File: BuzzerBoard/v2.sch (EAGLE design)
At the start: 9 parts, among them J1 p0, U1 LM386MX-1/NOPB

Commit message: starting on v2
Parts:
- removed R1: 23BR100KLFTR, BuzzerLib:23BR100KLFTR
- removed U$1: SMS-1308MS-2-R, BuzzerLib:SMS-1308MS-2-R
- added C5: GRM188R60J106ME47D, BuzzerLib:GRM188R60J106ME47D
- added C6: C2012X5R1A336M125AC, BuzzerLib:C2012X5R1A336M125AC
- added J2: (no value), SparkFun-Connectors:CONN_02
- added U2: Value, BuzzerLib:TPS63001DRCR
- added U3: LQM2HPN1R5MG0L, BuzzerLib:LQM2HPN1R5MG0L
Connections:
- removed net IN+: R1.2, U1.IN+
- new net 3V_REG: C6.1, U1.VS, U2.FB, U2.VOUT
- new net N$6: U2.L2, U3.2
- new net N$7: U2.L1, U3.1
- net +: now also J2.1; no longer U$1.+
- net 3.3V: now also C5.1, U2.EN, U2.PS_SYNC, U2.VIN, U2.VINA; no longer U1.VS
- net GND: now also C5.2, C6.2, J2.2, U2.GND, U2.PAD, U2.PGND; no longer R1.1, U$1.-
- net P0: now also U1.IN+; no longer R1.3
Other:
- moved on the sheet: J1

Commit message: progress on the v2 board
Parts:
- removed U2: Value, BuzzerLib:TPS63001DRCR
- removed U3: LQM2HPN1R5MG0L, BuzzerLib:LQM2HPN1R5MG0L
- added C7: 100nf, Seeed-Capacitor:CERAMIC-100NF-50V-10%-X7R(0603)
- added J3: inv, SparkFun-Connectors:CONN_02
- C5: value GRM188R60J106ME47D -> 100pf; device BuzzerLib:GRM188R60J106ME47D -> Seeed-Capacitor:CERAMIC-100PF-50V-5%-NPO(0603)
- C6: value C2012X5R1A336M125AC -> 100nf; device BuzzerLib:C2012X5R1A336M125AC -> Seeed-Capacitor:CERAMIC-100NF-50V-10%-X7R(0603)
- J1: value p0 -> input
- J2: value (none) -> speaker
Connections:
- removed net 3V_REG: C6.1, U1.VS, U2.FB, U2.VOUT
- removed net N$6: U2.L2, U3.2
- removed net N$7: U2.L1, U3.1
- new net IN-: J3.2, U1.IN-
- new net N$3: C5.1, J3.1
- net +: now also J2.2; no longer J2.1
- net 3.3V: now also C6.2, U1.VS; no longer C5.1, U2.EN, U2.PS_SYNC, U2.VIN, U2.VINA
- net GND: now also C6.1, C7.1, J2.1; no longer C6.2, J2.2, U1.IN-, U2.GND, U2.PAD, U2.PGND
- net P0: now also C7.2
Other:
- moved on the sheet: J1, J2

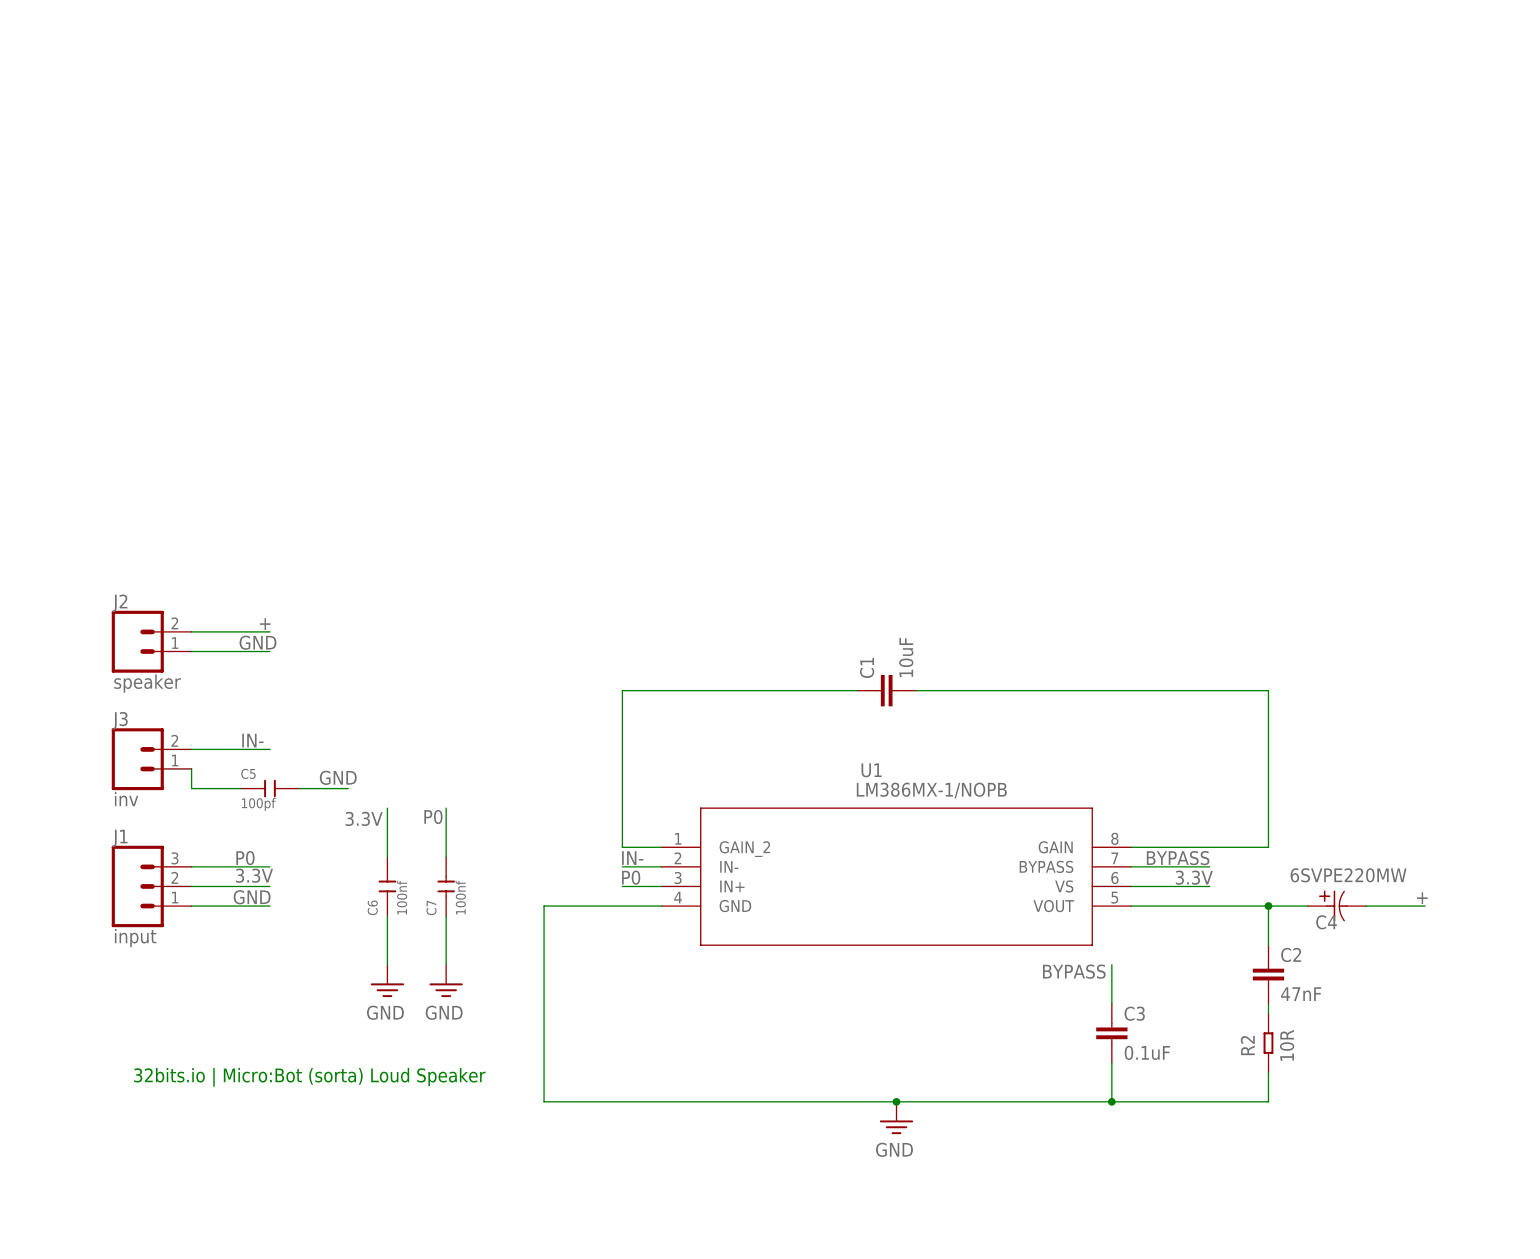
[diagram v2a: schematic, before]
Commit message: Switching to LM48310 on the v2 board.
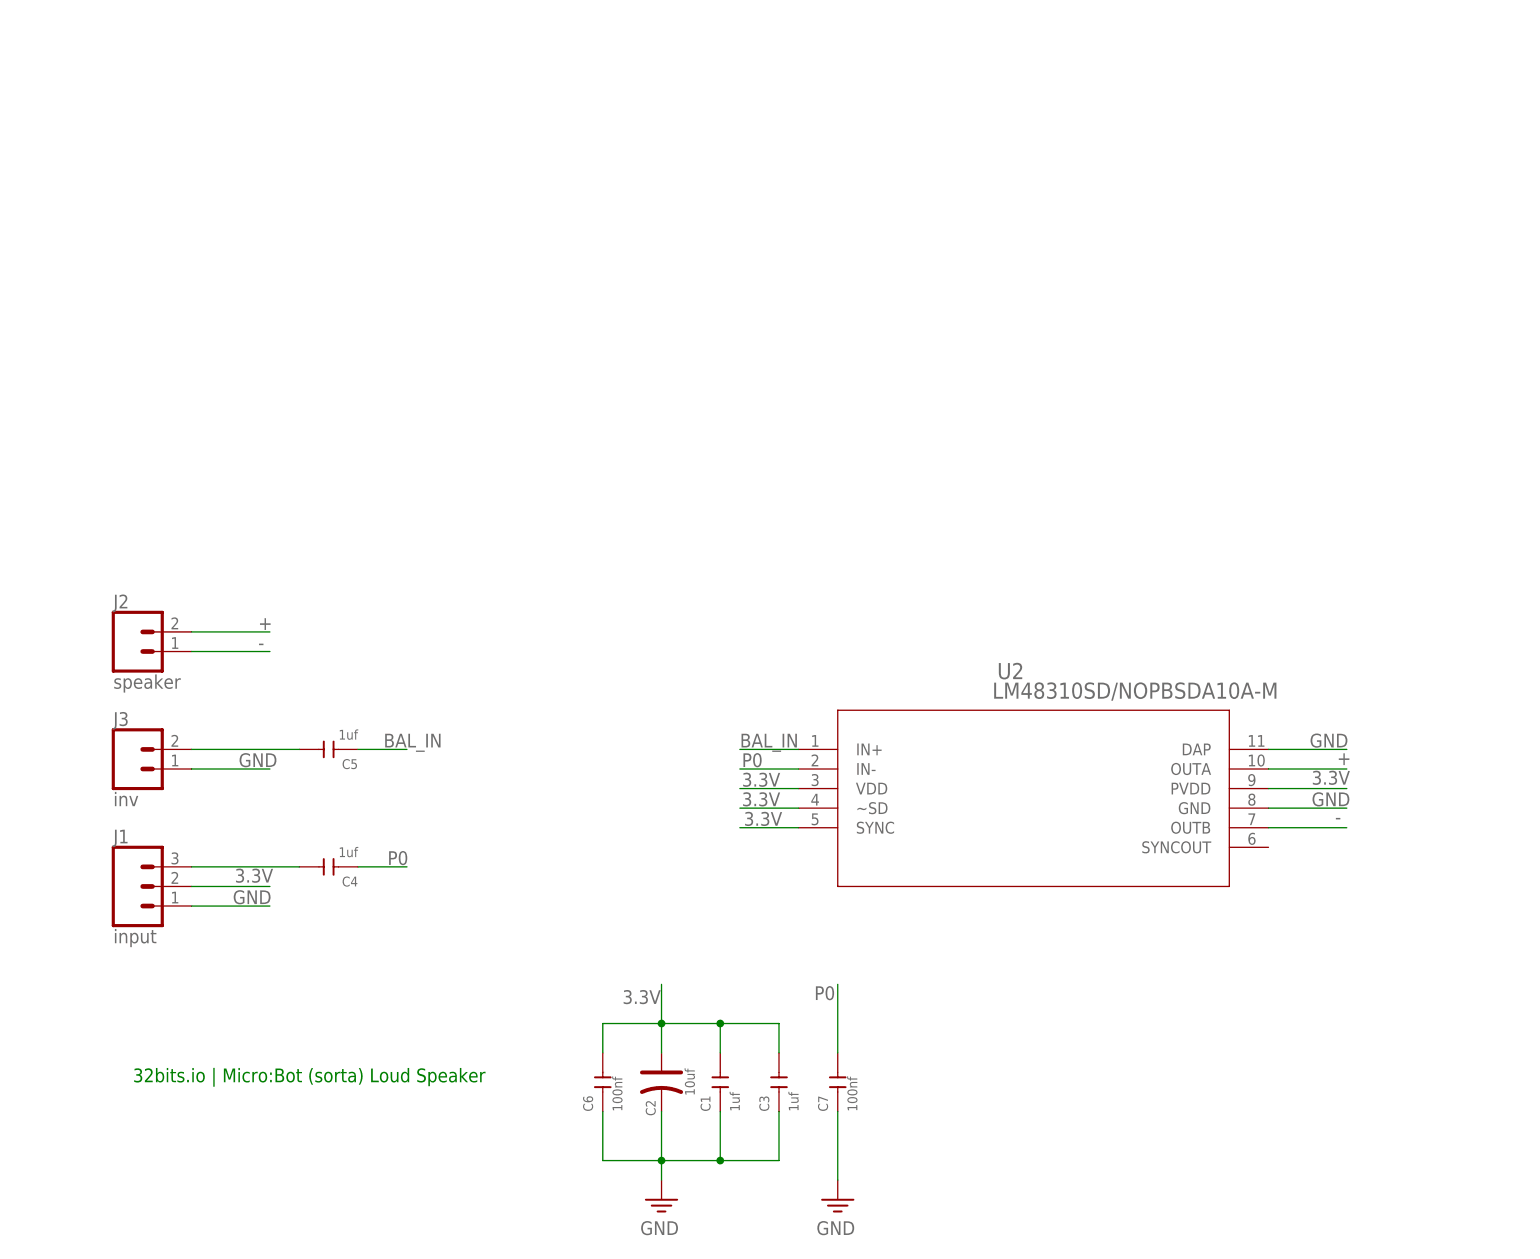
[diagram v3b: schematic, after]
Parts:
- removed R2: 10R, Seeed-Resistor:SMD-RES-0R-5%-1/10W(0603)
- removed U1: LM386MX-1/NOPB, BuzzerLib:LM386MX-1/NOPB
- added U2: LM48310SD/NOPBSDA10A-M, BuzzerLib:LM48310SD/NOPBSDA10A-M
- C1: value 10uF -> 1uf; device SparkFun-Capacitors:10UF-0603-6.3V-20% -> Seeed-Capacitor:CERAMIC-1UF-25V-10%-X7R(0603)
- C2: value 47nF -> 10uf; device SparkFun-Capacitors:47NF-0603-25V-5% -> Seeed-Capacitor:DIP-ALUMINUM-47UF-16V(D5-H7MM)
- C3: value 0.1uF -> 1uf; device SparkFun-Capacitors:0.1UF-0603-25V-(+80/-20%) -> Seeed-Capacitor:CERAMIC-1UF-25V-10%-X7R(0603)
- C4: value 6SVPE220MW -> 1uf; device BuzzerLib:6SVPE220MW -> Seeed-Capacitor:CERAMIC-1UF-25V-10%-X7R(0603); SPICEPREFIX C -> (none)
- C5: value 100pf -> 1uf; device Seeed-Capacitor:CERAMIC-100PF-50V-5%-NPO(0603) -> Seeed-Capacitor:CERAMIC-1UF-25V-10%-X7R(0603)
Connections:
- removed net BYPASS: C3.1, U1.BYPASS
- removed net GAIN: C1.2, U1.GAIN
- removed net IN-: J3.2, U1.IN-
- removed net N$1: C2.2, R2.2
- removed net N$2: C1.1, U1.GAIN_2
- removed net N$3: C5.1, J3.1
- removed net VOUT: C2.1, C4.11, U1.VOUT
- new net -: J2.1, U2.OUTB
- new net BAL_IN: C5.1, U2.IN+
- new net BAL_IN_RAW: C5.2, J3.2
- new net P0_RAW: C4.2, J1.3
- net +: now also U2.OUTA; no longer C4.22
- net 3.3V: now also C1.2, C2.+, C3.2, U2.PVDD, U2.SYNC, U2.VDD, U2.~SD; no longer U1.VS
- net GND: now also C1.1, C2.-, C3.1, J3.1, U2.DAP, U2.GND; no longer C3.2, C5.2, J2.1, R2.1, U1.GND
- net P0: now also C4.1, U2.IN-; no longer J1.3, U1.IN+
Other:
- moved on the sheet: C5, C6, C7
